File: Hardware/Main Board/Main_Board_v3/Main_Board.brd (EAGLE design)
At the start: 105.4 x 84.8 mm, 65 parts, among them IC1 MBED_MICROCONTROLLER, IC2 NE555, Q1 BS170, Q2 BS170, Q3 IRF3704L-V, Q4 IRF3704L-V, Q5 BS170, Q6 IRF3704L-V

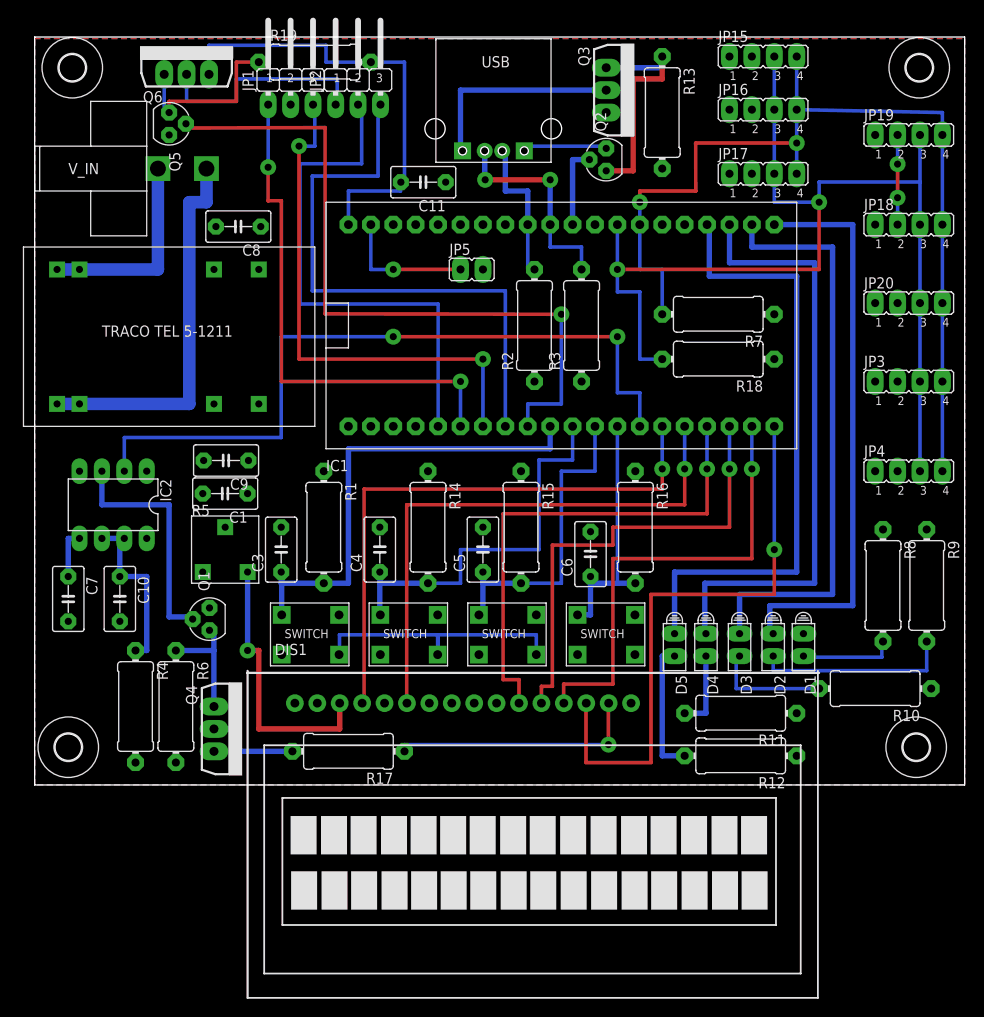
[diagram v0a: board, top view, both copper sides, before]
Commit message: Added power control of the LCD screen
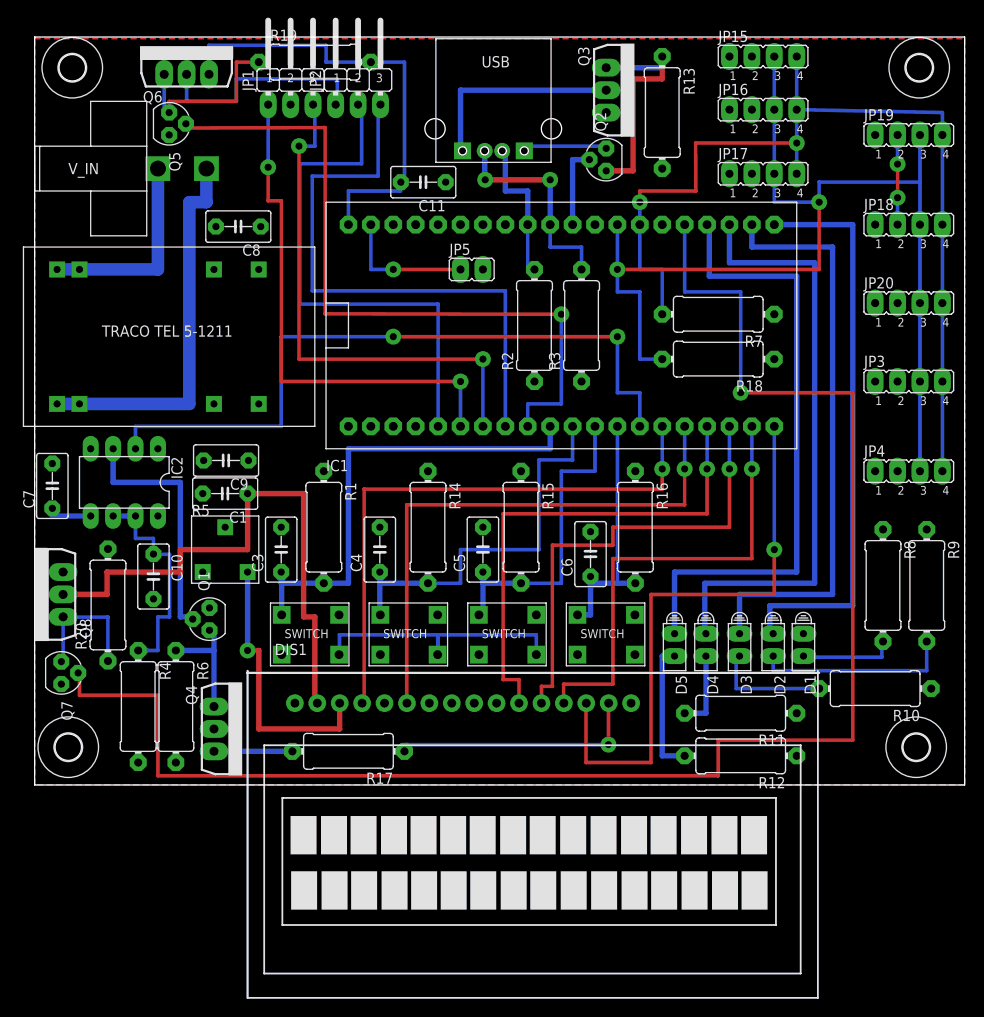
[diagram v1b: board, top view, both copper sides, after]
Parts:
- added Q7: BS170, transistor-small-signal:SOT54E
- added Q8: IRF3704L-V, transistor-power:TO262-V
- added R20: 1M, rcl:0411/12
- moved C7 12.9 mm to (4.55, 33.9), turned to 90 degrees
- moved C10 4.58 mm to (16.0, 23.6)
- moved IC2 2.84 mm to (12.7, 34.3)
- moved R4 0.30 mm to (14.3, 8.89)
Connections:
- new net N$10: Q7.D, Q8.1, R20.1
- new net P25: IC1.25, Q7.G
- new net VIN_LCD: C1.1, DIS1.2, Q8.2
- net GND: now also Q7.S
- net VIN: now also Q8.3, R20.2; no longer C1.1, DIS1.2
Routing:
- net P25: track 0.00 -> 180.8 mm, vias 0 -> 1
- net VIN_LCD: track 0.00 -> 64.0 mm
- net N$10: track 0.00 -> 15.4 mm
- net N$6: track 20.1 -> 25.2 mm
- net P14: track 83.8 -> 80.0 mm
- net N$11: track 27.1 -> 28.3 mm
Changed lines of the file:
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@@
 <element name="C8" library="capacitor-wima" package="C5B3.5" value="100nF" x="25.62" y="63.28" rot="R180"/>
 <element name="C9" library="capacitor-wima" package="C5B3.5" value="10uF" x="24.23" y="36.77" rot="R180"/>
-<element name="IC2" library="st-microelectronics" package="DIL-08" value="NE555" x="11.43" y="31.75" rot="R180">
-<attribute name="OC_NEWARK" value="89K1486" x="-82.55" y="114.3" size="1.778" layer="27" rot="R180" display="off"/>
-<attribute name="MPN" value="NE555N" x="-82.55" y="114.3" size="1.778" layer="27" rot="R180" display="off"/>
-<attribute name="MF" value="Arrow Electronics" x="-82.55" y="114.3" size="1.778" layer="27" rot="R180" display="off"/>
-<attribute name="OC_FARNELL" value="1467742" x="-82.55" y="114.3" size="1.778" layer="27" rot="R180" display="off"/>
+<element name="IC2" library="st-microelectronics" package="DIL-08" value="NE555" x="12.7" y="34.29" rot="R180">
+<attribute name="OC_NEWARK" value="89K1486" x="-81.28" y="116.84" size="1.778" layer="27" rot="R180" display="off"/>
+<attribute name="MPN" value="NE555N" x="-81.28" y="116.84" size="1.778" layer="27" rot="R180" display="off"/>
+<attribute name="MF" value="Arrow Electronics" x="-81.28" y="116.84" size="1.778" layer="27" rot="R180" display="off"/>
+<attribute name="OC_FARNELL" value="1467742" x="-81.28" y="116.84" size="1.778" layer="27" rot="R180" display="off"/>
 </element>
-<element name="C7" library="capacitor-wima" package="C5B3.5" value="10nF/0.01u" x="6.35" y="21.082" rot="R270"/>
-<element name="C10" library="capacitor-wima" package="C5B3.5" value="10n" x="12.192" y="21.082" rot="R270"/>
-<element name="R4" library="rcl" package="0411/12" value="300k" x="13.97" y="8.89" rot="R270"/>
+<element name="C7" library="capacitor-wima" package="C5B3.5" value="10nF/0.01u" x="4.5466" y="33.8836" rot="R90"/>
+<element name="C10" library="capacitor-wima" package="C5B3.5" value="10n" x="16.002" y="23.622" rot="R270"/>
+<element name="R4" library="rcl" package="0411/12" value="300k" x="14.2748" y="8.89" rot="R270"/>
 <element name="U$9" library="ekohub2013" package="TRACO_ISOLATED_SUPPLY" value="TRACO_ISOLATED_SUPPLY" x="5.08" y="43.18"/>
 <element name="U$4" library="ekohub2013" package="INPUT_VOLTAGE_CONNECTOR" value="INPUT_VOLTAGE_CONNECTOR" x="16.51" y="69.85"/>
@@
 <element name="R19" library="rcl" package="0411/12" value="1M" x="34.29" y="81.915"/>
 <element name="Q6" library="transistor-power" package="TO262-V" value="IRF3704L-V" x="19.76" y="80.53"/>
+<element name="Q7" library="transistor-small-signal" package="SOT54E" value="BS170" x="5.5626" y="12.7" rot="R270"/>
+<element name="R20" library="rcl" package="0411/12" value="1M" x="10.8458" y="20.3962" rot="R90"/>
+<element name="Q8" library="transistor-power" package="TO262-V" value="IRF3704L-V" x="5.7658" y="21.59" rot="R90"/>
 </elements>
 <signals>
@@
 <contactref element="C11" pad="1"/>
 <wire x1="83.82" y1="69.2658" x2="83.82" y2="69.85" width="0.4064" layer="1"/>
+<contactref element="Q7" pad="S"/>
 </signal>
 <signal name="VIN">
@@
 <contactref element="R13" pad="2"/>
 <contactref element="Q3" pad="3"/>
-<contactref element="DIS1" pad="2"/>
 <contactref element="U$7" pad="4"/>
 <contactref element="U$5" pad="4"/>
@@
 <contactref element="U$8" pad="4"/>
 <contactref element="D1" pad="A"/>
-<contactref element="C1" pad="1"/>
 <contactref element="R6" pad="2"/>
 <contactref element="Q4" pad="3"/>
@@
 <contactref element="R7" pad="1"/>
 <contactref element="JP5" pad="2"/>
+<contactref element="R20" pad="2"/>
+<contactref element="Q8" pad="3"/>
 </signal>
 <signal name="3V3_MBED">
@@
 <contactref element="IC2" pad="5"/>
 <contactref element="C7" pad="1"/>
-<wire x1="7.62" y1="27.94" x2="6.35" y2="27.94" width="0.6096" layer="16"/>
-<wire x1="6.35" y1="27.94" x2="6.35" y2="23.622" width="0.6096" layer="16"/>
+<wire x1="8.89" y1="30.48" x2="4.5466" y2="30.48" width="0.6096" layer="16"/>
+<wire x1="4.5466" y1="30.48" x2="4.5466" y2="31.3436" width="0.6096" layer="16"/>
 </signal>
 <signal name="N$6">
@@
 <contactref element="IC2" pad="6"/>
 <contactref element="IC2" pad="7"/>
-<wire x1="10.16" y1="27.94" x2="12.7" y2="27.94" width="0.6096" layer="16"/>
-<wire x1="12.7" y1="27.94" x2="12.192" y2="27.94" width="0.6096" layer="16"/>
-<wire x1="12.192" y1="27.94" x2="12.192" y2="23.622" width="0.6096" layer="16"/>
-<wire x1="12.192" y1="23.622" x2="15.24" y2="23.622" width="0.6096" layer="16"/>
-<wire x1="15.24" y1="23.622" x2="15.24" y2="15.24" width="0.6096" layer="16"/>
-<wire x1="15.24" y1="15.24" x2="13.97" y2="15.24" width="0.6096" layer="16"/>
+<wire x1="11.43" y1="30.48" x2="13.97" y2="30.48" width="0.6096" layer="16"/>
+<wire x1="15.24" y1="15.24" x2="14.2748" y2="15.24" width="0.6096" layer="16"/>
+<wire x1="13.97" y1="30.48" x2="13.97" y2="27.94" width="0.4064" layer="16"/>
+<wire x1="13.97" y1="27.94" x2="16.002" y2="27.94" width="0.4064" layer="16"/>
+<wire x1="16.002" y1="27.94" x2="16.002" y2="26.162" width="0.4064" layer="16"/>
+<wire x1="15.24" y1="15.24" x2="16.51" y2="15.24" width="0.4064" layer="16"/>
+<wire x1="16.51" y1="15.24" x2="16.51" y2="19.05" width="0.4064" layer="16"/>
+<wire x1="16.51" y1="19.05" x2="17.8308" y2="19.05" width="0.4064" layer="16"/>
+<wire x1="17.8308" y1="19.05" x2="17.8308" y2="26.1366" width="0.4064" layer="16"/>
+<wire x1="17.8308" y1="26.1366" x2="16.002" y2="26.1366" width="0.4064" layer="16"/>
+<wire x1="16.002" y1="26.1366" x2="16.002" y2="26.162" width="0.4064" layer="16"/>
 </signal>
 <signal name="N$8">
@@
 <contactref element="Q1" pad="G"/>
 <contactref element="IC2" pad="3"/>
-<wire x1="10.16" y1="35.56" x2="10.16" y2="31.75" width="0.6096" layer="16"/>
-<wire x1="10.16" y1="31.75" x2="17.78" y2="31.75" width="0.6096" layer="16"/>
-<wire x1="17.78" y1="31.75" x2="17.78" y2="19.05" width="0.6096" layer="16"/>
-<wire x1="17.78" y1="19.05" x2="20.447" y2="19.05" width="0.6096" layer="16"/>
+<wire x1="11.43" y1="38.1" x2="11.43" y2="34.29" width="0.6096" layer="16"/>
+<wire x1="11.43" y1="34.29" x2="19.05" y2="34.29" width="0.6096" layer="16"/>
+<wire x1="19.05" y1="34.29" x2="19.05" y2="19.05" width="0.6096" layer="16"/>
+<wire x1="19.05" y1="19.05" x2="20.447" y2="19.05" width="0.6096" layer="16"/>
 <wire x1="20.447" y1="19.05" x2="20.447" y2="18.796" width="0.6096" layer="16"/>
 </signal>
@@
 <via x="43.18" y="50.8" extent="1-16" drill="0.8" shape="square"/>
 <wire x1="43.18" y1="50.8" x2="30.48" y2="50.8" width="0.4064" layer="16"/>
-<wire x1="30.48" y1="50.8" x2="30.48" y2="39.37" width="0.4064" layer="16"/>
-<wire x1="30.48" y1="39.37" x2="12.7" y2="39.37" width="0.4064" layer="16"/>
-<wire x1="12.7" y1="39.37" x2="12.7" y2="35.56" width="0.4064" layer="16"/>
+<wire x1="30.48" y1="50.8" x2="30.48" y2="40.64" width="0.4064" layer="16"/>
+<wire x1="30.48" y1="40.64" x2="13.97" y2="40.64" width="0.4064" layer="16"/>
+<wire x1="13.97" y1="40.64" x2="13.97" y2="38.1" width="0.4064" layer="16"/>
 <wire x1="71.12" y1="40.64" x2="71.12" y2="44.45" width="0.4064" layer="16"/>
 <wire x1="71.12" y1="44.45" x2="68.58" y2="44.45" width="0.4064" layer="16"/>
@@
 <wire x1="19.76" y1="77.47" x2="19.76" y2="80.53" width="0.4064" layer="16"/>
 </signal>
+<signal name="N$10">
+<contactref element="Q7" pad="D"/>
+<contactref element="Q8" pad="1"/>
+<contactref element="R20" pad="1"/>
+<wire x1="5.5626" y1="13.97" x2="5.7658" y2="13.97" width="0.4064" layer="16"/>
+<wire x1="5.7658" y1="13.97" x2="5.7658" y2="19.05" width="0.4064" layer="16"/>
+<wire x1="10.8458" y1="14.0462" x2="10.8458" y2="19.0246" width="0.4064" layer="16"/>
+<wire x1="10.8458" y1="19.0246" x2="5.7658" y2="19.0246" width="0.4064" layer="16"/>
+<wire x1="5.7658" y1="19.0246" x2="5.7658" y2="19.05" width="0.4064" layer="16"/>
+</signal>
+<signal name="VIN_LCD">
+<contactref element="DIS1" pad="2"/>
+<contactref element="C1" pad="1"/>
+<contactref element="Q8" pad="2"/>
+<wire x1="34.57" y1="9.27" x2="34.29" y2="9.27" width="0.6096" layer="1"/>
+<wire x1="34.29" y1="9.27" x2="34.29" y2="19.05" width="0.6096" layer="1"/>
+<wire x1="34.29" y1="19.05" x2="33.02" y2="19.05" width="0.6096" layer="1"/>
+<wire x1="33.02" y1="19.05" x2="33.02" y2="33.02" width="0.6096" layer="1"/>
+<wire x1="33.02" y1="33.02" x2="26.67" y2="33.02" width="0.6096" layer="1"/>
+<wire x1="26.67" y1="33.02" x2="26.67" y2="26.67" width="0.6096" layer="1"/>
+<wire x1="26.67" y1="26.67" x2="19.05" y2="26.67" width="0.6096" layer="1"/>
+<wire x1="19.05" y1="26.67" x2="19.05" y2="24.13" width="0.6096" layer="1"/>
+<wire x1="19.05" y1="24.13" x2="10.7442" y2="24.13" width="0.6096" layer="1"/>
+<wire x1="10.7442" y1="24.13" x2="10.7442" y2="21.59" width="0.6096" layer="1"/>
+<wire x1="10.7442" y1="21.59" x2="5.7658" y2="21.59" width="0.6096" layer="1"/>
+</signal>
+<signal name="P25">
+<contactref element="Q7" pad="G"/>
+<contactref element="IC1" pad="25"/>
+<wire x1="76.2" y1="63.5" x2="76.2" y2="55.88" width="0.4064" layer="16"/>
+<wire x1="76.2" y1="55.88" x2="82.55" y2="55.88" width="0.4064" layer="16"/>
+<wire x1="82.55" y1="55.88" x2="82.55" y2="44.45" width="0.4064" layer="16"/>
+<via x="82.55" y="44.45" extent="1-16" drill="0.8" shape="square"/>
+<wire x1="82.55" y1="44.45" x2="95.25" y2="44.45" width="0.4064" layer="1"/>
+<wire x1="95.25" y1="44.45" x2="95.25" y2="5.08" width="0.4064" layer="1"/>
+<wire x1="95.25" y1="5.08" x2="80.01" y2="5.08" width="0.4064" layer="1"/>
+<wire x1="80.01" y1="5.08" x2="80.01" y2="1.0414" width="0.4064" layer="1"/>
+<wire x1="80.01" y1="1.0414" x2="16.51" y2="1.0414" width="0.4064" layer="1"/>
+<wire x1="16.51" y1="1.0414" x2="16.51" y2="10.16" width="0.4064" layer="1"/>
+<wire x1="16.51" y1="10.16" x2="7.62" y2="10.16" width="0.4064" layer="1"/>
+<wire x1="7.62" y1="10.16" x2="7.62" y2="12.7" width="0.4064" layer="1"/>
+<wire x1="7.62" y1="12.7" x2="7.4676" y2="12.7" width="0" layer="19" extent="1-1"/>
+</signal>
 </signals>
